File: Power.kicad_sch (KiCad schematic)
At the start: 25 parts, among them IC2 LM66200DRLR, Q1 ???, U4 TPS631000DRLR, U5 MCP73831-2-OT

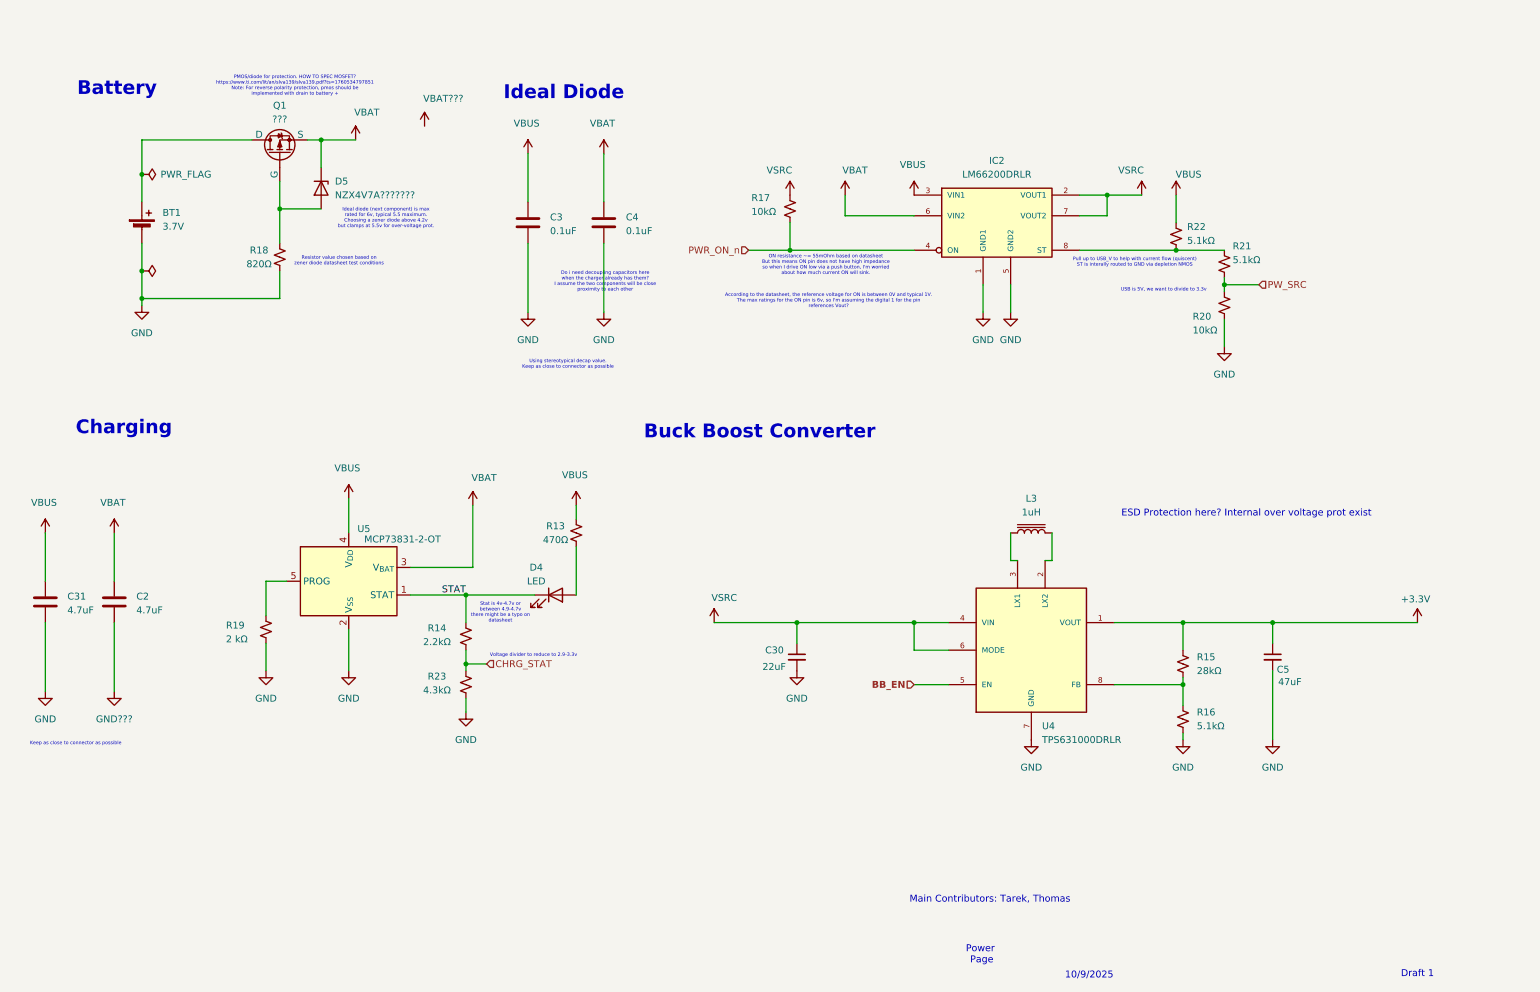
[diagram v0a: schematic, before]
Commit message: Draft 2 Revision 2
Footprints still not all assigned.

Added: Test points, zero resistors, battery voltage monitor IC, PTC and zener surge protection on VBUS, UART connector

Changed: rerouted some signals, removed zener and resistor for reverse pol bat protection
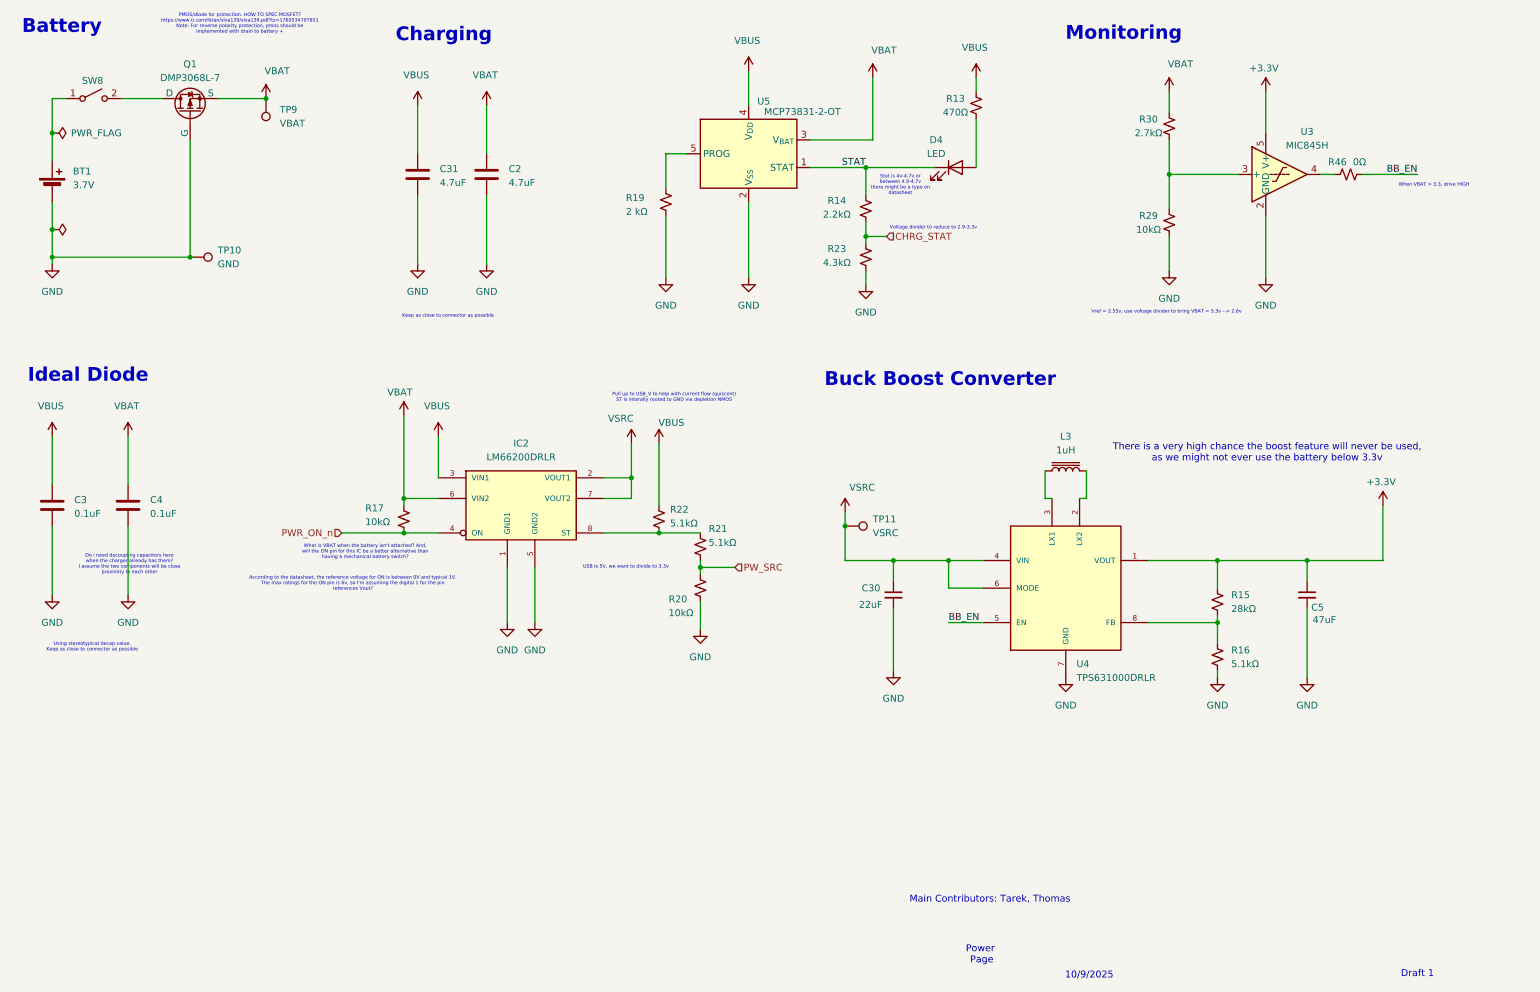
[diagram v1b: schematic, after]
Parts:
- removed D5: NZX4V7A???????, ???, symbol Device:D_Zener
- removed R18: 820Ω, symbol Device:R_Small_US
- added R29: 10kΩ, Resistor_SMD:R_0805_2012Metric, symbol Device:R_Small_US
- added R30: 2.7kΩ, Resistor_SMD:R_0805_2012Metric, symbol Device:R_Small_US
- added R46: 0Ω, Resistor_SMD:R_0805_2012Metric, symbol Device:R_Small_US
- added SW8: SW_SPST, Button_Switch_SMD:SW_DIP_SPSTx01_Slide_6.7x4.1mm_W8.61mm_P2.54mm_LowProfile, symbol Switch:SW_SPST
- added TP10: GND, symbol Connector:TestPoint
- added TP11: VSRC, symbol Connector:TestPoint
- added TP9: VBAT, symbol Connector:TestPoint
- added U3: MIC845H, Package_TO_SOT_SMD:SOT-353_SC-70-5, symbol Comparator:MIC845H
- Q1: value ??? -> DMP3068L-7
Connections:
- net GND??? is gone; now on net GND: C2.1
- net +3.3V: now also U3.5 (V+)
- net BB_EN: now also R46.2
- net GND: now also Q1.2 (G), R29.1, TP10.1, U3.2 (GND)
- net VBAT: now also R17.1, R30.2, TP9.1
- net VSRC: now also TP11.1; no longer R17.1
- net at BT1.1 (+): now also SW8.1 (A); no longer Q1.1 (D)
- new net: Q1.1 (D), SW8.2 (B)
- new net: R46.1, U3.4
- new net: R29.2, R30.1, U3.3 (+)
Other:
- note added: "Monitoring"
- note added: "There is a very high chance the boost feature will never be used, as we might not ever use the battery below 3.3v"
- note added: "Vref = 2.55v, use voltage divider to bring VBAT = 3.3v --> 2.6v"
- note added: "What is VBAT when the battery isn't attached? And, will the ON pin for this IC be a better alternative than having a mechanical battery switch?"
- note added: "When VBAT > 3.3, drive HIGH"
- note removed: "ESD Protection here? Internal over voltage prot exist"
- note removed: "Ideal diode (next component) is max rated for 6v, typical 5.5 maximum. Choosing a zener diode above 4.2v but clamps at 5.5v for over-voltage prot."
- note removed: "ON resistance ~= 55mOhm based on datasheet But this means ON pin does not have high impedance so when I drive ON low via a push button, I'm worried about how much current ON will sink."
- note removed: "Resistor value chosen based on zener diode datasheet test conditions"
- moved on the sheet: BT1, C2, C3, C30, C31, C4, C5, D4, IC2, L3, Q1, R13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

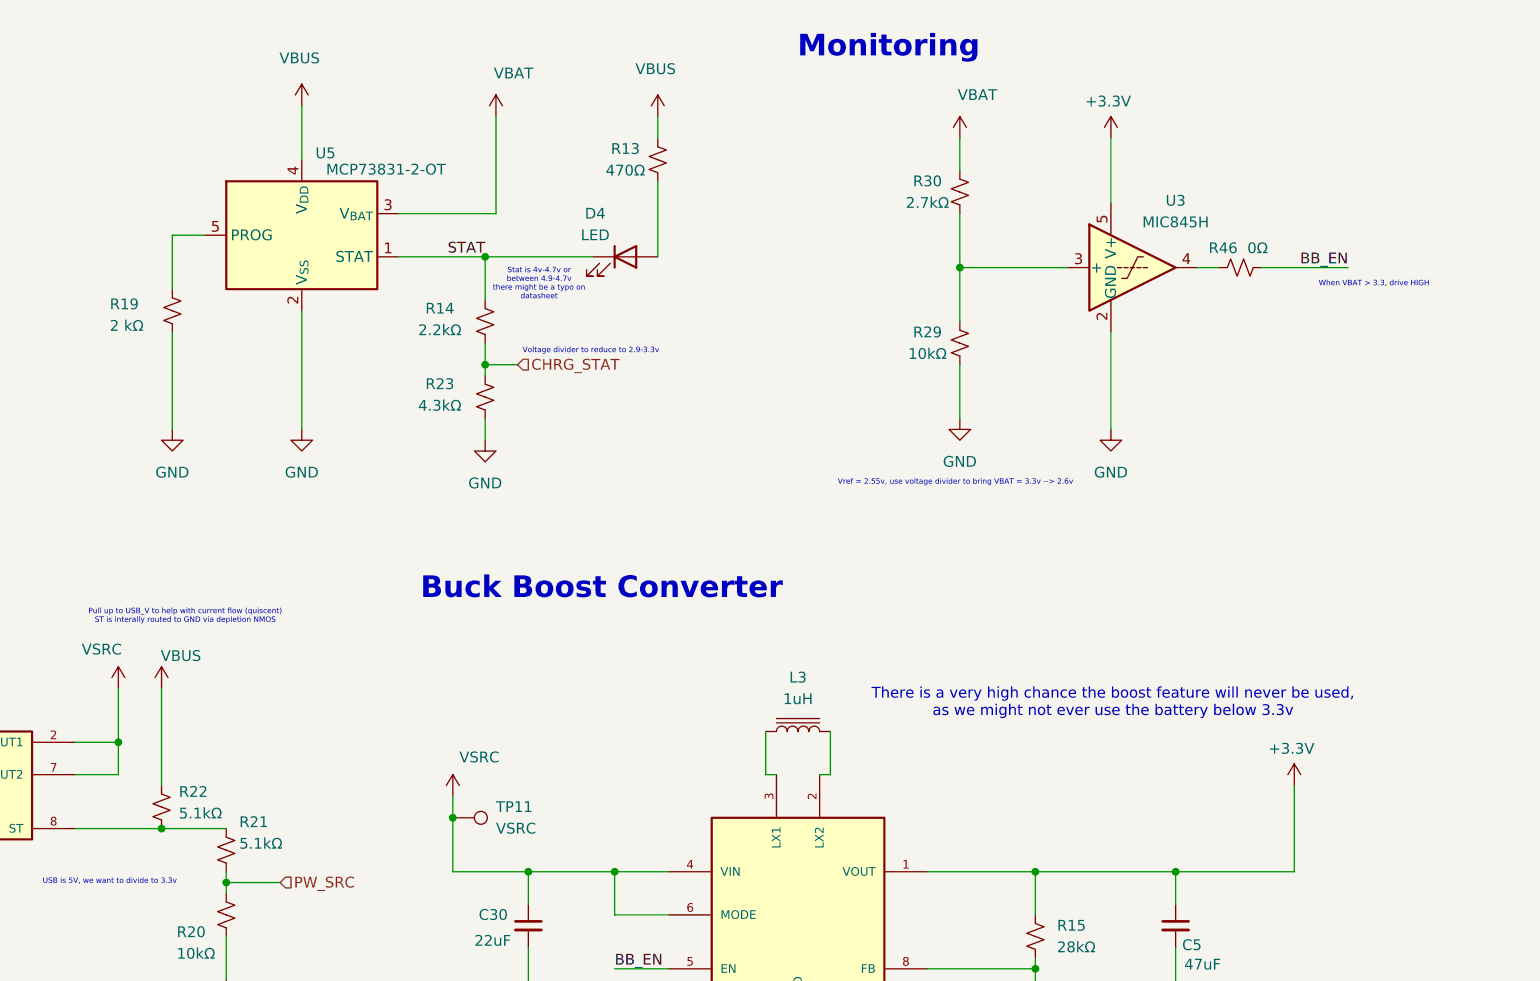
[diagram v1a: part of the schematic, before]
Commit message: Remaining Footprint Added
Beware of footprints that come from online but do not match the kicad libraries - the pins might be mapped wrong!
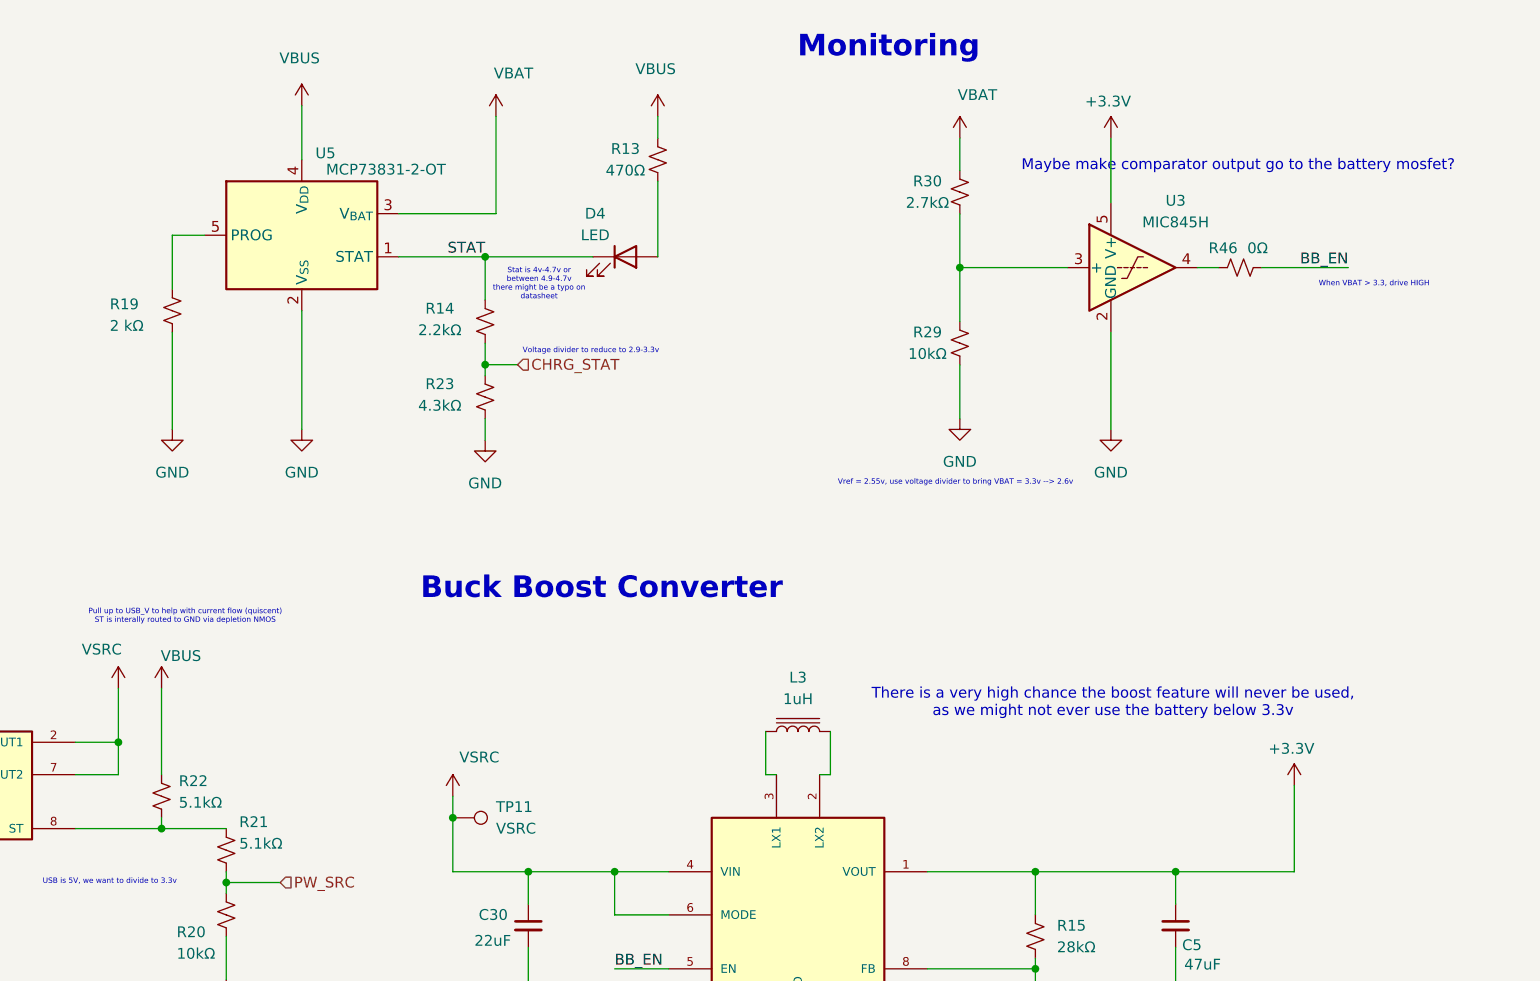
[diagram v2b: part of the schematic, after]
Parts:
- BT1: footprint Connector_JST:JST_GH_SM02B-GHS-TB_1x02-1MP_P1.25mm_Horizontal -> Connector_JST:JST_PH_B2B-PH-K_1x02_P2.00mm_Vertical
- C2, C3: footprint Resistor_SMD:R_0805_2012Metric -> Capacitor_SMD:C_0805_2012Metric_Pad1.18x1.45mm_HandSolder
- C4: footprint (none) -> Capacitor_SMD:C_0805_2012Metric_Pad1.18x1.45mm_HandSolder
- D4: footprint (none) -> LED_SMD:LED_0805_2012Metric_Pad1.15x1.40mm_HandSolder
- L3: footprint Inductor_SMD:L_1008_2520Metric -> Inductor_SMD:L_0805_2012Metric_Pad1.05x1.20mm_HandSolder
- Q1: footprint Package_TO_SOT_SMD:SOT-23-6_Handsoldering -> Package_TO_SOT_SMD:SOT-23-3
- R16, R17, R19, R21, R23: footprint (none) -> Resistor_SMD:R_0805_2012Metric
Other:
- note added: "Maybe make comparator output go to the battery mosfet?"
- moved on the sheet: R22
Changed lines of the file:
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@@
 		)
 	)
+	(text "Maybe make comparator output go to the battery mosfet?"
+		(exclude_from_sim no)
+		(at 260.096 33.782 0)
+		(effects
+			(font
+				(size 1.27 1.27)
+			)
+		)
+	)
 	(text "Stat is 4v-4.7v or \nbetween 4.9-4.7v\nthere might be a typo on\ndatasheet"
 		(exclude_from_sim no)
@@
 	(wire
 		(pts
+			(xy 133.35 110.49) (xy 133.35 111.76)
+		)
+		(stroke
+			(width 0)
+			(type default)
+		)
+	)
+	(wire
+		(pts
 			(xy 176.53 116.84) (xy 186.69 116.84)
 		)
@@
 	(wire
 		(pts
-			(xy 133.35 95.25) (xy 133.35 106.68)
+			(xy 133.35 95.25) (xy 133.35 105.41)
 		)
 		(stroke
@@
 			)
 		)
-		(property "Footprint" "Package_TO_SOT_SMD:SOT-23-6_Handsoldering"
+		(property "Footprint" "Package_TO_SOT_SMD:SOT-23-3"
 			(at 44.45 29.21 0)
 			(effects
@@
 			)
 		)
-		(property "Footprint" "Resistor_SMD:R_0805_2012Metric"
+		(property "Footprint" "Capacitor_SMD:C_0805_2012Metric_Pad1.18x1.45mm_HandSolder"
 			(at 20.6248 102.87 0)
 			(effects
@@
 			)
 		)
-		(property "Footprint" ""
+		(property "Footprint" "Resistor_SMD:R_0805_2012Metric"
 			(at 86.36 109.22 0)
 			(effects
@@
 			)
 		)
-		(property "Footprint" ""
+		(property "Footprint" "LED_SMD:LED_0805_2012Metric_Pad1.15x1.40mm_HandSolder"
 			(at 187.96 44.45 0)
 			(effects
@@
 			)
 		)
-		(property "Footprint" "Inductor_SMD:L_1008_2520Metric"
+		(property "Footprint" "Inductor_SMD:L_0805_2012Metric_Pad1.05x1.20mm_HandSolder"
 			(at 208.28 100.33 0)
 			(effects
@@
 			)
 		)
-		(property "Footprint" ""
+		(property "Footprint" "Resistor_SMD:R_0805_2012Metric"
 			(at 134.62 50.8 0)
 			(effects
@@
 		(on_board yes)
 		(dnp no)
-		(fields_autoplaced yes)
 		(property "Reference" "BT1"
 			(at 25.4 45.1484 0)
@@
 			)
 		)
-		(property "Footprint" "Connector_JST:JST_GH_SM02B-GHS-TB_1x02-1MP_P1.25mm_Horizontal"
+		(property "Footprint" "Connector_JST:JST_PH_B2B-PH-K_1x02_P2.00mm_Vertical"
 			(at 21.59 46.736 90)
 			(effects
@@
 	(symbol
 		(lib_id "Device:R_Small_US")
-		(at 133.35 109.22 0)
+		(at 133.35 107.95 0)
 		(unit 1)
 		(exclude_from_sim no)
@@
 		(dnp no)
 		(property "Reference" "R22"
-			(at 135.382 107.442 0)
+			(at 135.382 106.172 0)
 			(effects
 				(font
@@
 		)
 		(property "Value" "5.1kΩ"
-			(at 135.382 109.982 0)
+			(at 135.382 108.712 0)
 			(effects
 				(font
@@
 		)
 		(property "Footprint" "Resistor_SMD:R_0805_2012Metric"
-			(at 133.35 109.22 0)
+			(at 133.35 107.95 0)
 			(effects
 				(font
@@
 		)
 		(property "Datasheet" "~"
-			(at 133.35 109.22 0)
+			(at 133.35 107.95 0)
 			(effects
 				(font
@@
 		)
 		(property "Description" "Resistor, small US symbol"
-			(at 133.35 109.22 0)
+			(at 133.35 107.95 0)
 			(effects
 				(font
@@
 			)
 		)
-		(property "Footprint" ""
+		(property "Footprint" "Resistor_SMD:R_0805_2012Metric"
 			(at 140.97 114.3 0)
 			(effects
@@
 			)
 		)
-		(property "Footprint" "Resistor_SMD:R_0805_2012Metric"
+		(property "Footprint" "Capacitor_SMD:C_0805_2012Metric_Pad1.18x1.45mm_HandSolder"
 			(at 100.6348 41.91 0)
 			(effects
@@
 			)
 		)
-		(property "Footprint" ""
+		(property "Footprint" "Capacitor_SMD:C_0805_2012Metric_Pad1.18x1.45mm_HandSolder"
 			(at 34.5948 102.87 0)
 			(effects
@@
 			)
 		)
-		(property "Footprint" ""
+		(property "Footprint" "Resistor_SMD:R_0805_2012Metric"
 			(at 236.22 134.62 0)
 			(effects
@@
 			)
 		)
-		(property "Footprint" ""
+		(property "Footprint" "Resistor_SMD:R_0805_2012Metric"
 			(at 171.45 60.96 0)
 			(effects

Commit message: Components Placed on Layout
Added Power Management PMOS, Assigned missing footprints
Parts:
- TP10, TP11, TP9: footprint (none) -> TestPoint:TestPoint_Pad_1.5x1.5mm
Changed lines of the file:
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@@
 	(text "PMOS/diode for protection. HOW TO SPEC MOSFET?\nhttps://www.ti.com/lit/an/slva139/slva139.pdf?ts=1760534797851\nNote: For reverse polarity protection, pmos should be\nimplemented with drain to battery +"
 		(exclude_from_sim no)
-		(at 56.134 18.034 0)
+		(at 49.53 19.05 0)
 		(effects
 			(font
@@
 			)
 		)
-		(property "Footprint" ""
+		(property "Footprint" "TestPoint:TestPoint_Pad_1.5x1.5mm"
 			(at 55.88 31.75 0)
 			(effects
@@
 			)
 		)
-		(property "Footprint" ""
+		(property "Footprint" "TestPoint:TestPoint_Pad_1.5x1.5mm"
 			(at 167.64 115.57 0)
 			(effects
@@
 			)
 		)
-		(property "Footprint" ""
+		(property "Footprint" "TestPoint:TestPoint_Pad_1.5x1.5mm"
 			(at 46.99 66.04 0)
 			(effects
